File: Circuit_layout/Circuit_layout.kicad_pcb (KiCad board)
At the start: 2 copper layers, 168 parts, among them CON1 AVR-JTAG-10, J1 Spare_Conns, J10 AIRs, J3 CAN, J4 Motor_Ctrl, J5 RJ12, P1 TSV, P2 HVPL, P3 IMD, P4 GLV, P5 Cockpit, P6 Pedals, P7 BrakeLight/RTDS, Q1 MMBF170, Q2 MMBF170, Q3 BSS84, SW1 TS5A3159-Q1, U1 LM7332, U10 MCP2551-I/SN, U11 TLP293, U12 TLP293, U13 PDQ10-D, U14 PDQ15-D, U15 TLP293, U16 LTC3638, U17 MCP6004, U18 PDQ10-Q24-S12-D, U19 ACPL-C870, U2 LM7810CT, U20 ACPL-C870, U21 MCP6001, U3 MCP6004, U4 MCP6004, U5 LM7332, U6 LM339, U7 AT90CAN128-A, U8 74ACT11030, U9 TLP293, Y1 10MHz

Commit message: started working on throttle layout in pcb. added ch_gnd plane
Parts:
- removed C13, C36, C39: 0.1u, Capacitors_SMD:C_0805_HandSoldering
- removed C20: 15p, Capacitors_SMD:C_0805_HandSoldering
- removed C21, C9: 6.8uF, Capacitors_SMD:C_0805_HandSoldering
- removed C48: 10uF, Capacitors_SMD:C_0805_HandSoldering
- removed C8: 1uF, Capacitors_SMD:C_2220_HandSoldering
- removed R17: 150, Resistors_SMD:R_0805_HandSoldering
- removed R21: 1k, Resistors_SMD:R_0805_HandSoldering
- removed R85: 2k, Resistors_SMD:R_0805_HandSoldering
- removed R86: 100, Resistors_SMD:R_0805_HandSoldering
- removed U14: PDQ15-D, custom_footprints:PDQ_DCDC
- removed U4: MCP6004, Housings_SOIC:SOIC-14_3.9x8.7mm_Pitch1.27mm
- added HVPL_HV1: TEST_1P, Measurement_Points:Measurement_Point_Round-SMD-Pad_Big, F.Cu at (278.1, 29.2)
- added JP1: JUMPER3, Pin_Headers:Pin_Header_Straight_1x03_Pitch2.54mm, F.Cu at (78.7, 62.2)
- added L1: 100uH, Inductors:Inductor_Taiyo-Yuden_NR-80xx_HandSoldering, F.Cu at (247.7, 64.8)
- added R69: 250k, Resistors_SMD:R_0805_HandSoldering, F.Cu at (251.5, 43.2)
- added R70: 47k, Resistors_SMD:R_0805_HandSoldering, F.Cu at (260.4, 48.3)
- added R71: 330, Resistors_SMD:R_0805_HandSoldering, F.Cu at (188.0, 86.4)
- added R72: 330, Resistors_SMD:R_0805_HandSoldering, F.Cu at (153.7, 87.6)
- added R73: 330, Resistors_SMD:R_0805_HandSoldering, F.Cu at (158.8, 69.8)
- added R74: 330, Resistors_SMD:R_0805_HandSoldering, F.Cu at (153.7, 74.9)
- added R76: 750k, Resistors_SMD:R_0805_HandSoldering, F.Cu at (245.1, 55.9)
- added R77: 196k, Resistors_SMD:R_0805_HandSoldering, F.Cu at (251.5, 55.9)
- added SW2: TS5A3159-Q1, TO_SOT_Packages_SMD:SOT-23-6_Handsoldering, F.Cu at (-24.1, 139.7)
- added SW3: JS202011CQN, custom_footprints:CK_DPDT_Switch, F.Cu at (39.4, -11.4)
- added U22: TS372, Housings_SOIC:SOIC-8_3.9x4.9mm_Pitch1.27mm, F.Cu at (69.8, 88.9)
- added U23: TLP293, Housings_SSOP:SOP-4_4.4x2.8mm_Pitch1.27mm, F.Cu at (-17.8, 97.8)
- added U24: TLP293, Housings_SSOP:SOP-4_4.4x2.8mm_Pitch1.27mm, F.Cu at (-27.9, 97.8)
- added W1: I_Measure, Measurement_Points:Measurement_Point_Round-SMD-Pad_Big, F.Cu at (110.5, 31.8)
- added W10: Throttle_LPF, Measurement_Points:Measurement_Point_Round-SMD-Pad_Big, F.Cu at (31.8, 119.4)
- added W11: Throttle_LV, Measurement_Points:Measurement_Point_Round-SMD-Pad_Big, F.Cu at (-22.9, 149.9)
- added W12: V_Measure, Measurement_Points:Measurement_Point_Round-SMD-Pad_Big, F.Cu at (217.2, 71.1)
- added W13: Throttle_HV, Measurement_Points:Measurement_Point_Round-SMD-Pad_Big, F.Cu at (248.9, 134.6)
- added W14: +5HV, Measurement_Points:Measurement_Point_Round-SMD-Pad_Big, F.Cu at (227.3, 135.9)
- added W15: I/O_Ground, Measurement_Points:Measurement_Point_Round-SMD-Pad_Big, F.Cu at (232.4, 147.3)
- added W16: +24V, Measurement_Points:Measurement_Point_Round-SMD-Pad_Big, F.Cu at (66.0, 35.6)
- added W17: CH_GND, Measurement_Points:Measurement_Point_Square-SMD-Pad_Big, F.Cu at (55.9, 121.9)
- added W18: HV_GND, Measurement_Points:Measurement_Point_Square-SMD-Pad_Big, F.Cu at (257.8, 59.7)
- added W19: HVPL_LV, Measurement_Points:Measurement_Point_Round-SMD-Pad_Big, F.Cu at (247.7, 29.2)
- added W2: IMD_uC, Measurement_Points:Measurement_Point_Round-SMD-Pad_Big, F.Cu at (199.4, 96.5)
- added W20: GLV_GND, Measurement_Points:Measurement_Point_Square-SMD-Pad_Big, F.Cu at (55.9, 130.8)
- added W21: +5DC/DC_GND, Measurement_Points:Measurement_Point_Square-SMD-Pad_Big, F.Cu at (48.3, 130.8)
- added W22: +5DC/DC, Measurement_Points:Measurement_Point_Round-SMD-Pad_Big, F.Cu at (129.5, 111.8)
- added W23: V_Meas_GND, Measurement_Points:Measurement_Point_Square-SMD-Pad_Big, F.Cu at (48.3, 121.9)
- added W3: uC_GND, Measurement_Points:Measurement_Point_Square-SMD-Pad_Big, F.Cu at (38.1, 130.8)
- added W4: +10_GND, Measurement_Points:Measurement_Point_Square-SMD-Pad_Big, F.Cu at (33.0, 130.8)
- added W5: +10V, Measurement_Points:Measurement_Point_Round-SMD-Pad_Big, F.Cu at (-55.9, 114.3)
- added W6: APPS2_b, Measurement_Points:Measurement_Point_Round-SMD-Pad_Big, F.Cu at (-74.9, 147.3)
- added W7: APPS1_b, Measurement_Points:Measurement_Point_Round-SMD-Pad_Big, F.Cu at (-61.0, 114.3)
- added W8: Throttle_uC, Measurement_Points:Measurement_Point_Round-SMD-Pad_Big, F.Cu at (105.4, 99.1)
- added W9: Throttle_PL, Measurement_Points:Measurement_Point_Round-SMD-Pad_Big, F.Cu at (90.2, 67.3)
- C22: value DNP -> 0.1u
- C23: value 10uF -> 0.1u
- C24: value 15p -> 1uF; footprint Capacitors_SMD:C_0805_HandSoldering -> Capacitors_SMD:C_2220_HandSoldering
- C3: value 0.1u -> 2.2uF
- P7: value BrakeLight/RTDS -> RTDS; footprint custom_footprints:TerminalBlock_Pheonix_MPT-5.08mm_4pol -> custom_footprints:TerminalBlock_Pheonix_MPT-5.08mm_2pol
- Q1: value MMBF170 -> ZVP4525G; footprint TO_SOT_Packages_SMD:SOT-23 -> TO_SOT_Packages_SMD:SOT-223-3Lead_TabPin2
- Q3: value BSS84 -> MMBF170
- R1, R13, R22, R23, R28, R29, R3, R31, R4, R6, R7: value 1k -> 10k
- R14: value 47k -> 10k
- R16: value 2k -> 250k
- R18: value 100 -> 10k
- R19, R20: value 100 -> 250k
- R2: value 1k -> 250k
- R24, R30: value 1k -> 100k
- R39: value 750k -> 10k
- R42: value 196k -> 10k
- R51, R52: value 0 -> 250k
- R8: value 1M -> 10k
- SW1: value TS5A3159-Q1 -> SW_PUSH; footprint TO_SOT_Packages_SMD:SOT-23-6_Handsoldering -> custom_footprints:SW_RACON_8
- U1: value LM7332 -> PDM2-S24-S12; footprint Housings_SOIC:SOIC-8_3.9x4.9mm_Pitch1.27mm -> Converters_DCDC_ACDC:DCDC-Conv_TRACO_TMR_1-xxxx_Single
- U18: value PDQ10-Q24-S12-D -> TS912; footprint custom_footprints:PDQ_DCDC -> Housings_SOIC:SOIC-8_3.9x4.9mm_Pitch1.27mm
- U2: value LM7810CT -> MCP6002; footprint TO_SOT_Packages_THT:TO-220_Vertical -> Housings_SOIC:SOIC-8_3.9x4.9mm_Pitch1.27mm
- U5: value LM7332 -> LM7810CT; footprint Housings_SOIC:SOIC-8_3.9x4.9mm_Pitch1.27mm -> Power_Integrations:TO-220
- U6: value LM339 -> TS912; footprint Housings_SOIC:SOIC-14_3.9x8.7mm_Pitch1.27mm -> Housings_SOIC:SOIC-8_3.9x4.9mm_Pitch1.27mm
- moved C24 237.1 mm to (275.6, 49.5)
- moved U1 220.9 mm to (262.9, 17.8)
- moved R39 185.0 mm to (54.6, 82.5), turned to 270 degrees
- moved U18 181.5 mm to (52.1, 88.9)
- moved R42 178.1 mm to (59.7, 80.0)
- moved C23 177.5 mm to (55.9, 71.1)
- moved C15 118.1 mm to (-35.3, 109.9)
- moved R51 118.1 mm to (-13.0, 104.3)
- moved R52 118.1 mm to (-24.9, 115.4)
- moved C14 118.1 mm to (-40.3, 115.5)
- moved C44 118.1 mm to (-33.3, 104.3)
- moved R25 73.6 mm to (33.0, 92.7), turned to 90 degrees
- moved R30 72.2 mm to (44.5, 73.7)
- moved U2 67.6 mm to (96.5, 110.5)
- moved SW1 67.4 mm to (115.6, 63.5)
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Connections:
- C15 pad 1: APPS1 -> I_+5
- C16 pad 1: APPS2 -> Net-(C16-Pad1)
- C18 pad 1: +5V -> I_+5
- C22 pad 1: /Status Lights/BP_uC -> Net-(C22-Pad1)
- C23 pad 1: Net-(C19-Pad1) -> APPS1_10
- C23 pad 2: /Status Lights/HV- -> CH_GND
- C24 pad 1: Net-(C24-Pad1) -> /Status Lights/HV+
- C24 pad 2: CH_GND -> /Status Lights/HV-
- C25 pad 1: +5V -> I_+5
- C27 pad 1: +5V -> I_+5
- C3 pad 1: IMD_PWM -> HVPL
- C32 pad 1: +5V -> I_+5
- C33 pad 1: +5V -> I_+5
- C37 pad 1: +5V -> I_+5
- C38 pad 1: +5V -> APPS1_10
- C42 pad 1: +5V -> I_+5
- C43 pad 1: +5V -> I_+5
- C44 pad 1: +5V -> I_+5
- C45 pad 1: +5V -> I_+5
- C7 pad 1: +5V -> I_+5
- CON1 pad 4: +5V -> I_+5
- CON1 pad 7: Net-(CON1-Pad7) -> (no net)
- CON1 pad 8: Net-(CON1-Pad8) -> (no net)
- J5 pad 1: Net-(J5-Pad1) -> (no net)
- J5 pad 4: CH_GND -> I_RTN
- J5 pad 5: +5V -> I_+5
- J5 pad 6: Net-(J5-Pad6) -> (no net)
- P5 pad 3: +5V -> I_+5
- P6 pad 2: BP -> BOT
- P6 pad 3: APPS1_10 -> BP
- P6 pad 4: APPS2_5 -> APPS1_10
- P6 pad 5: APPS1_RTN -> APPS2_5
- P6 pad 6: CH_GND -> APPS1_RTN
- P6 pad 7: APPS1 -> CH_GND
- P6 pad 8: APPS2 -> APPS1
- P7 pad 1: Brake_Light -> RTDS
- P7 pad 2: RTDS -> CH_GND
- Q1 pad 2: CH_GND -> IMD_Fault_LED
- Q1 pad 3: Brake_Light -> +24V
- Q3 pad 2: IMD_Fault_LED -> CH_GND
- Q3 pad 3: +12V -> I_RTN
- R1 pad 1: CH_GND -> Net-(R1-Pad1)
- R1 pad 2: Net-(R1-Pad2) -> CH_GND
- R10 pad 1: +5V -> I_+5
- R11 pad 1: SDA -> SCL
- R11 pad 2: +5V -> I_+5
- R13 pad 1: Net-(Q1-Pad1) -> I_+5
- R13 pad 2: /Status Lights/BP_uC -> ~RESET_AVR
- R14 pad 1: Net-(R14-Pad1) -> Net-(Q3-Pad1)
- R14 pad 2: /Status Lights/HV- -> /I_ENB
- R16 pad 1: +24V -> Net-(R16-Pad1)
- R16 pad 2: Net-(R16-Pad2) -> /Status Lights/HV+
- R18 pad 1: +5V -> CH_GND
- R18 pad 2: Net-(D1-Pad2) -> Net-(Q3-Pad1)
- R19 pad 1: /Status Lights/Spare_Red -> Net-(R19-Pad1)
- R19 pad 2: Net-(D3-Pad2) -> Net-(R16-Pad1)
- R2 pad 1: Net-(R2-Pad1) -> AIRs+
- R2 pad 2: A1_LV -> Net-(R2-Pad2)
- R20 pad 1: /Status Lights/Spare_Blue -> Net-(R20-Pad1)
- R20 pad 2: Net-(D4-Pad2) -> Net-(R19-Pad1)
- R22 pad 1: Net-(R22-Pad1) -> /ThrottlePlausibility/APPS1_b
- R22 pad 2: +5V -> Net-(R22-Pad2)
- R23 pad 1: Net-(R21-Pad1) -> I_+5
- R23 pad 2: CH_GND -> Net-(R23-Pad2)
- R24 pad 1: /ThrottlePlausibility/APPS1_ISO -> APPS2
- R24 pad 2: Net-(R22-Pad1) -> Net-(C16-Pad1)
- R28 pad 1: Net-(R28-Pad1) -> Net-(R22-Pad2)
- R28 pad 2: APPS1 -> CH_GND
- R29 pad 1: Net-(R29-Pad1) -> Net-(R23-Pad2)
- R29 pad 2: APPS2 -> /ThrottlePlausibility/APPS1_ISO
- R3 pad 2: A2_LV -> A1_LV
- R30 pad 1: Net-(R28-Pad1) -> APPS1
- R30 pad 2: CH_GND -> Net-(C22-Pad1)
- R31 pad 1: Net-(R31-Pad1) -> /ThrottlePlausibility/APPS1_b
- R31 pad 2: Net-(R29-Pad1) -> Net-(R31-Pad2)
- R39 pad 1: Net-(C19-Pad1) -> /ThrottlePlausibility/APPS2_b
- R4 pad 1: Net-(R2-Pad1) -> Net-(R4-Pad1)
- R4 pad 2: CH_GND -> A2_LV
- R40 pad 1: Net-(C20-Pad1) -> Net-(R40-Pad1)
- R40 pad 2: +5V -> I_+5
- R41 pad 1: Net-(C24-Pad1) -> Net-(R41-Pad1)
- R41 pad 2: +5V -> I_+5
- R42 pad 1: Net-(R39-Pad2) -> Net-(R31-Pad2)
- R42 pad 2: /Status Lights/HV- -> CH_GND
- R43 pad 1: SCL -> /ThrottlePlausibility/Throttle_SEL
- R43 pad 2: +5V -> CH_GND
- R46 pad 2: APPS2 -> /ThrottlePlausibility/APPS2_b
- R47 pad 2: +5V -> I_+5
- R5 pad 2: +5V -> I_+5
- R50 pad 1: CH_GND -> Net-(R39-Pad2)
- R50 pad 2: BP -> Net-(R50-Pad2)
- R51 pad 2: /Status Lights/BP_uC -> Net-(R51-Pad2)
- R52 pad 1: CH_GND -> BOT
- R52 pad 2: CH_GND -> Net-(R52-Pad2)
- R6 pad 1: /I_Measure -> CH_GND
- R7 pad 1: Net-(R7-Pad1) -> /I_Measure
- R7 pad 2: AIRs+ -> Net-(R4-Pad1)
- R79 pad 2: +5V -> I_+5
- R8 pad 1: /Status Lights/HV+ -> SDA
- R8 pad 2: Net-(R14-Pad1) -> I_+5
- R82 pad 2: +5V -> I_+5
- R84 pad 1: Net-(Q3-Pad1) -> Net-(Q1-Pad1)
- SW1 pad 1: /ThrottlePlausibility/Pedal_Out -> ~RESET_AVR
- U1 pad 1: /ThrottlePlausibility/APPS1_ISO -> /Status Lights/HV-
- U1 pad 2: Net-(R22-Pad1) -> Net-(C19-Pad1)
- U1 pad 4: CH_GND -> (no net)
- U10 pad 3: +5V -> I_+5
- U10 pad 5: Net-(U10-Pad5) -> (no net)
- U11 pad 4: Net-(R16-Pad2) -> +24V
- U13 pad 3: +5V -> I_+5
- U13 pad 4: Net-(U13-Pad4) -> (no net)
- U13 pad 6: Net-(U13-Pad6) -> (no net)
- U15 pad 2: Net-(R1-Pad2) -> Net-(R1-Pad1)
- U16 pad 14: Net-(R14-Pad1) -> Net-(R69-Pad1)
- U16 pad 9: Net-(R39-Pad2) -> Net-(R76-Pad2)
- U17 pad 12: Net-(R79-Pad1) -> (no net)
- U17 pad 13: /ThrottlePlausibility/APPS1_ISO -> (no net)
- U17 pad 14: Net-(U17-Pad14) -> (no net)
- U17 pad 2: Net-(R3-Pad1) -> Net-(R4-Pad1)
- U17 pad 3: Net-(R2-Pad1) -> Net-(R3-Pad1)
- U17 pad 4: +5V -> I_+5
- U18 pad 1: /Status Lights/HV- -> /ThrottlePlausibility/APPS1_ISO
- U18 pad 2: Net-(C19-Pad1) -> Net-(R23-Pad2)
- U18 pad 3: /Status Lights/HVPL -> Net-(R22-Pad2)
- U18 pad 4: Net-(U18-Pad4) -> CH_GND
- U18 pad 5: CH_GND -> Net-(R31-Pad2)
- U18 pad 6: (no net) -> Net-(R39-Pad2)
- U19 pad 1: +5V -> I_+5
- U2 pad 1: +24V -> /ThrottlePlausibility/Pedal_Out
- U2 pad 2: CH_GND -> /ThrottlePlausibility/Pedal_Out
- U2 pad 3: APPS1_10 -> Net-(Q2-Pad3)
- U20 pad 8: +5V -> I_+5
- U3 pad 10: APPS2 -> Net-(R38-Pad1)
- U3 pad 12: (no net) -> /ThrottlePlausibility/APPS2_b
- U3 pad 13: (no net) -> Net-(R38-Pad2)
- U3 pad 14: (no net) -> Net-(U3-Pad14)
- U3 pad 2: Net-(R80-Pad2) -> /ThrottlePlausibility/APPS1_ISO
- U3 pad 3: /ThrottlePlausibility/APPS1_ISO -> Net-(R79-Pad1)
- U3 pad 4: +5V -> I_+5
- U3 pad 5: Net-(R38-Pad1) -> /ThrottlePlausibility/APPS1_ISO
- U3 pad 6: APPS2 -> Net-(R80-Pad2)
- U3 pad 9: Net-(R38-Pad2) -> /ThrottlePlausibility/APPS2_b
- U5 pad 1: Net-(R31-Pad1) -> +24V
- U5 pad 2: Net-(R29-Pad1) -> CH_GND
- U5 pad 3: Net-(R28-Pad1) -> APPS1_10
- U6 pad 1: Net-(C24-Pad1) -> /ThrottlePlausibility/APPS1_b
- U6 pad 2: Net-(C20-Pad1) -> /ThrottlePlausibility/APPS1_b
- U6 pad 3: APPS1_10 -> Net-(C22-Pad1)
- U6 pad 4: Net-(R31-Pad1) -> CH_GND
- U6 pad 5: Net-(R32-Pad1) -> Net-(C16-Pad1)
- U6 pad 6: Net-(R33-Pad1) -> /ThrottlePlausibility/APPS2_b
- U6 pad 7: Net-(R31-Pad1) -> /ThrottlePlausibility/APPS2_b
- U6 pad 8: (no net) -> APPS1_10
- U7 pad 10: Net-(U7-Pad10) -> (no net)
- U7 pad 11: Net-(U7-Pad11) -> (no net)
- U7 pad 12: Net-(U7-Pad12) -> (no net)
- U7 pad 13: Net-(U7-Pad13) -> (no net)
- U7 pad 14: /Status Lights/BP_uC -> /ThrottlePlausibility/BP_uC
- U7 pad 18: Net-(U7-Pad18) -> (no net)
- U7 pad 19: Net-(U7-Pad19) -> (no net)
- U7 pad 21: +5V -> I_+5
- U7 pad 27: Net-(U7-Pad27) -> (no net)
- U7 pad 28: Net-(U7-Pad28) -> (no net)
- U7 pad 29: Net-(U7-Pad29) -> (no net)
- U7 pad 32: Net-(U7-Pad32) -> (no net)
- U7 pad 33: Net-(U7-Pad33) -> (no net)
- U7 pad 34: Net-(U7-Pad34) -> (no net)
- U7 pad 35: Net-(U7-Pad35) -> /ThrottlePlausibility/BOT_uC
- U7 pad 39: Net-(U7-Pad39) -> (no net)
- U7 pad 4: Net-(U7-Pad4) -> (no net)
- U7 pad 40: Net-(U7-Pad40) -> (no net)
- U7 pad 41: Net-(U7-Pad41) -> (no net)
- U7 pad 42: Net-(U7-Pad42) -> (no net)
- U7 pad 43: Net-(U7-Pad43) -> (no net)
- U7 pad 44: Net-(U7-Pad44) -> /I_ENB
- U7 pad 45: Net-(U7-Pad45) -> (no net)
- U7 pad 49: Net-(U7-Pad49) -> (no net)
- U7 pad 50: Net-(U7-Pad50) -> (no net)
- U7 pad 51: /Safety_Loop -> (no net)
- U7 pad 52: +5V -> I_+5
- U7 pad 54: TDI -> /PIN54
- U7 pad 55: TDO -> /PIN55
- U7 pad 6: Net-(U7-Pad6) -> (no net)
- U7 pad 64: +5V -> I_+5
- U7 pad 7: Net-(U7-Pad7) -> /Safety_Loop
- U7 pad 8: Net-(U7-Pad8) -> (no net)
- U8 pad 1: +5V -> I_+5
- U8 pad 11: +5V -> I_+5
- U8 pad 12: Net-(U3-Pad1) -> Net-(U3-Pad7)
- U8 pad 13: Net-(U3-Pad7) -> Net-(U3-Pad8)
- U8 pad 14: Net-(U3-Pad8) -> Net-(U3-Pad14)
- U8 pad 2: +5V -> I_+5
- U8 pad 3: Net-(C20-Pad1) -> Net-(R40-Pad1)
- U8 pad 8: Net-(C24-Pad1) -> Net-(R41-Pad1)
- U8 pad 9: Net-(U17-Pad14) -> Net-(U3-Pad1)
- U9 pad 1: Net-(R7-Pad1) -> Net-(R2-Pad2)
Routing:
- net I_+5: track 0.00 -> 12.8 mm
- net /ThrottlePlausibility/APPS1_b: track 0.00 -> 9.92 mm
- net Net-(C16-Pad1): track 0.00 -> 8.84 mm
- net /ThrottlePlausibility/APPS2_b: track 0.00 -> 8.72 mm
- net /ThrottlePlausibility/Throttle_PL: track 0.00 -> 5.41 mm
- net Net-(Q2-Pad1): track 0.00 -> 3.81 mm
- net APPS1_10: track 0.00 -> 3.23 mm
- added copper zone on F.Cu, net CH_GND
- added copper zone on F.Cu, net HV-
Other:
- board outline added: 203.2 x 152.4 mm

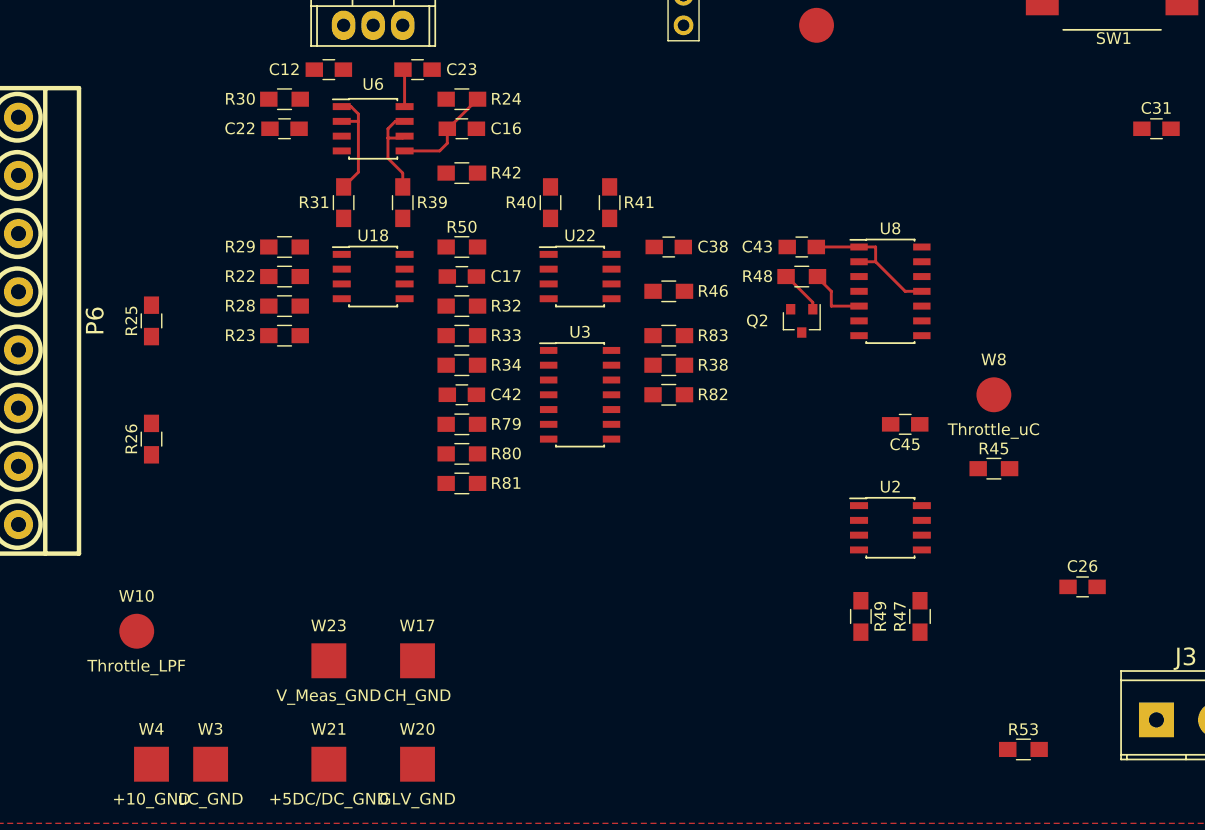
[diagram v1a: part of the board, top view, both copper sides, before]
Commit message: reviewed schematic w/ prof. nadovich. proposed changes
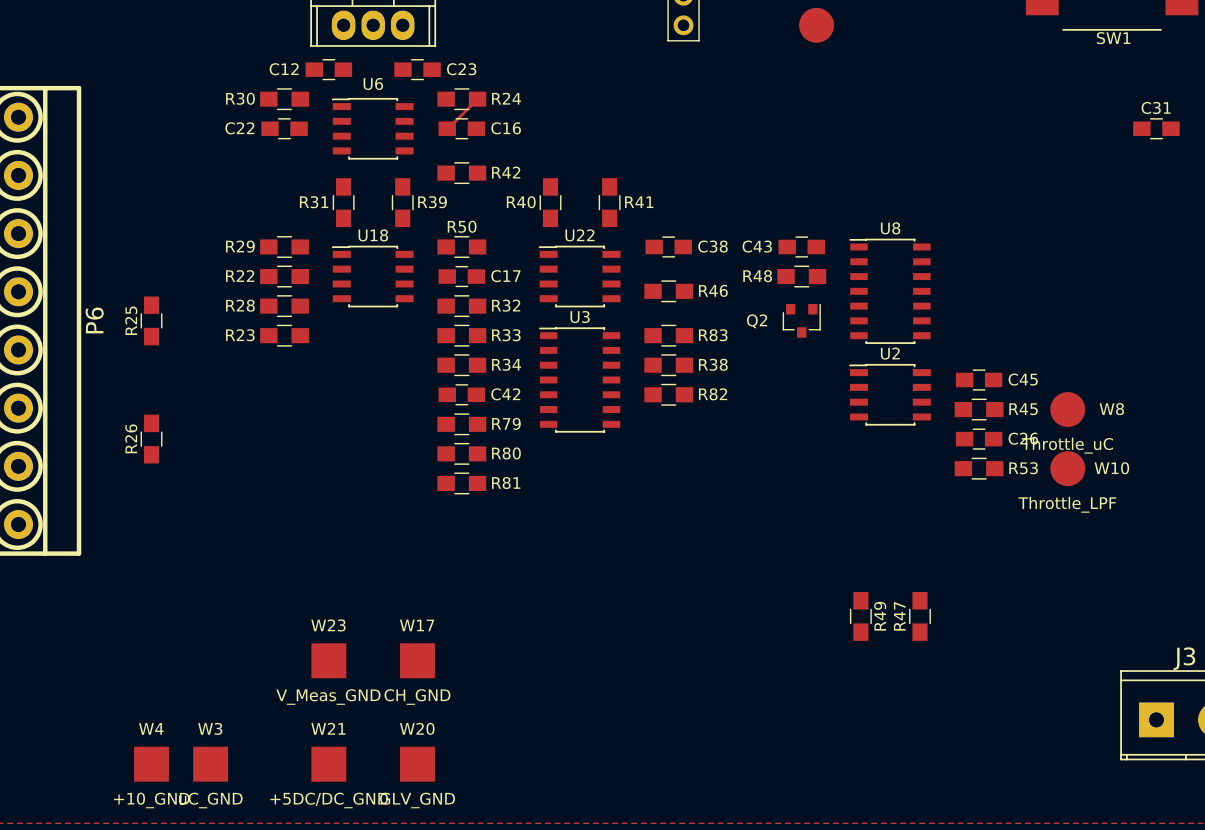
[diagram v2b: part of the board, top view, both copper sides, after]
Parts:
- moved W10 81.2 mm to (111.8, 105.4)
- moved R53 24.4 mm to (104.1, 105.4)
- moved C26 15.5 mm to (104.1, 102.9), turned to 180 degrees
- moved U2 11.4 mm to (96.5, 99.1)
- moved C45 7.41 mm to (104.1, 97.8), turned to 0 degrees
- moved W8 6.48 mm to (111.8, 100.3)
- moved R45 5.24 mm to (104.1, 100.3), turned to 180 degrees
- moved U3 1.27 mm to (69.8, 97.8)
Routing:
- net I_+5: track 12.8 -> 0.00 mm
- net /ThrottlePlausibility/APPS1_b: track 9.92 -> 0.00 mm
- net /ThrottlePlausibility/APPS2_b: track 8.72 -> 0.23 mm
- net /ThrottlePlausibility/Throttle_PL: track 5.41 -> 0.08 mm
- net Net-(C16-Pad1): track 8.84 -> 3.65 mm
- net Net-(Q2-Pad1): track 3.81 -> 0.08 mm
- net APPS1_10: track 3.23 -> 0.20 mm

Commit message: small changes
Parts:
- moved W18 130.4 mm to (170.2, 156.2)
- moved C40 89.8 mm to (175.6, 149.7)
- moved C41 89.8 mm to (179.3, 153.7)
- moved R60 89.8 mm to (183.1, 153.7)
- moved R61 89.8 mm to (186.9, 157.5)
- moved R65 89.8 mm to (193.2, 157.5)
- moved R67 89.8 mm to (199.6, 157.5)
- moved R68 89.8 mm to (205.9, 157.5)
- moved U20 68.4 mm to (185.4, 139.7), turned to 90 degrees
- moved C28 49.6 mm to (178.9, 115.8)
- moved C29 49.6 mm to (178.9, 130.8)
- moved C33 49.6 mm to (191.9, 128.8)
- moved R54 49.6 mm to (178.9, 120.8)
- moved R55 49.6 mm to (178.9, 125.8)
- moved R56 49.6 mm to (185.9, 125.8)
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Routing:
- net HV-: track 13.6 -> 0.14 mm
- net Net-(C41-Pad1): track 12.4 -> 0.14 mm
- net Net-(R67-Pad2): track 3.65 -> 0.00 mm
- net Net-(R61-Pad2): track 3.65 -> 0.00 mm
- net Net-(R65-Pad2): track 3.65 -> 0.00 mm
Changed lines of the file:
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@@
   (general
     (links 405)
-    (no_connects 330)
+    (no_connects 328)
     (area -78.419286 -19.055 282.071667 165.175001)
     (thickness 1.6)
     (drawings 9)
-    (tracks 24)
+    (tracks 9)
     (zones 0)
     (modules 193)
@@
     (pad_to_mask_clearance 0.2)
     (aux_axis_origin 0 0)
-    (visible_elements 7FFEFFFF)
+    (visible_elements 7FFEF7FF)
     (pcbplotparams
       (layerselection 0x00030_80000001)
@@
   )
   (module Capacitors_SMD:C_0805_HandSoldering (layer F.Cu)
-    (at 244.04 91.44 90)
+    (at 179.27 153.67 90)
     (descr "Capacitor SMD 0805, hand soldering")
     (tags "capacitor 0805")
@@
   )
   (module custom_footprints:Iso_Diff_Amp_ACPL (layer F.Cu)
-    (at 233.88 91.44 180)
+    (at 185.42 139.7 90)
     (descr "8-Lead Plastic Small Outline (SM) - Medium, 5.28 mm Body [SOIC] (see Microchip Packaging Specification 00000049BS.pdf)")
     (tags "SOIC 1.27")
     (attr smd)
-    (fp_text reference U20 (at 0 -3.68 180) (layer F.SilkS)
+    (fp_text reference U20 (at 0 -3.68 90) (layer F.SilkS)
       (effects (font (size 1 1) (thickness 0.15)))
     )
-    (fp_text value ACPL-C870 (at 0 3.68 180) (layer F.Fab)
+    (fp_text value ACPL-C870 (at 0 3.68 90) (layer F.Fab)
       (effects (font (size 1 1) (thickness 0.15)))
     )
@@
     (fp_line (start -2.75 -2.755) (end 2.75 -2.755) (layer F.SilkS) (width 0.15))
     (fp_line (start -2.75 2.755) (end 2.75 2.755) (layer F.SilkS) (width 0.15))
-    (pad 1 smd rect (at -5.3725 -1.905 180) (size 1.905 0.64) (layers F.Cu F.Paste F.Mask)
+    (pad 1 smd rect (at -5.3725 -1.905 90) (size 1.905 0.64) (layers F.Cu F.Paste F.Mask)
       (net 24 +5HV))
-    (pad 2 smd rect (at -5.3725 -0.635 180) (size 1.905 0.64) (layers F.Cu F.Paste F.Mask)
+    (pad 2 smd rect (at -5.3725 -0.635 90) (size 1.905 0.64) (layers F.Cu F.Paste F.Mask)
       (net 27 "Net-(C41-Pad1)"))
-    (pad 3 smd rect (at -5.3725 0.635 180) (size 1.905 0.64) (layers F.Cu F.Paste F.Mask)
+    (pad 3 smd rect (at -5.3725 0.635 90) (size 1.905 0.64) (layers F.Cu F.Paste F.Mask)
       (net 26 HV-))
-    (pad 4 smd rect (at -5.3725 1.905 180) (size 1.905 0.64) (layers F.Cu F.Paste F.Mask)
+    (pad 4 smd rect (at -5.3725 1.905 90) (size 1.905 0.64) (layers F.Cu F.Paste F.Mask)
       (net 26 HV-))
-    (pad 5 smd rect (at 5.3725 1.905 180) (size 1.905 0.65) (layers F.Cu F.Paste F.Mask)
+    (pad 5 smd rect (at 5.3725 1.905 90) (size 1.905 0.65) (layers F.Cu F.Paste F.Mask)
       (net 1 CH_GND))
-    (pad 6 smd rect (at 5.3725 0.635 180) (size 1.905 0.65) (layers F.Cu F.Paste F.Mask)
+    (pad 6 smd rect (at 5.3725 0.635 90) (size 1.905 0.65) (layers F.Cu F.Paste F.Mask)
       (net 81 "Net-(R57-Pad1)"))
-    (pad 7 smd rect (at 5.3725 -0.635 180) (size 1.905 0.64) (layers F.Cu F.Paste F.Mask)
+    (pad 7 smd rect (at 5.3725 -0.635 90) (size 1.905 0.64) (layers F.Cu F.Paste F.Mask)
       (net 21 "Net-(C29-Pad1)"))
-    (pad 8 smd rect (at 5.3725 -1.905 180) (size 1.905 0.64) (layers F.Cu F.Paste F.Mask)
+    (pad 8 smd rect (at 5.3725 -1.905 90) (size 1.905 0.64) (layers F.Cu F.Paste F.Mask)
       (net 108 I_+5))
     (model Housings_SOIC.3dshapes/SOIJ-8_5.3x5.3mm_Pitch1.27mm.wrl
@@
   )
   (module Capacitors_SMD:C_0805_HandSoldering (layer F.Cu)
-    (at 209 95)
+    (at 204.47 92.71)
     (descr "Capacitor SMD 0805, hand soldering")
     (tags "capacitor 0805")
@@
   )
   (module Capacitors_SMD:C_0805_HandSoldering (layer F.Cu)
-    (at 217 84)
+    (at 178.9 115.75)
     (descr "Capacitor SMD 0805, hand soldering")
     (tags "capacitor 0805")
@@
   )
   (module Capacitors_SMD:C_0805_HandSoldering (layer F.Cu)
-    (at 217 99 180)
+    (at 178.9 130.75 180)
     (descr "Capacitor SMD 0805, hand soldering")
     (tags "capacitor 0805")
@@
   )
   (module Capacitors_SMD:C_0805_HandSoldering (layer F.Cu)
-    (at 230 97 180)
+    (at 191.9 128.75 180)
     (descr "Capacitor SMD 0805, hand soldering")
     (tags "capacitor 0805")
@@
   )
   (module Capacitors_SMD:C_0805_HandSoldering (layer F.Cu)
-    (at 240.4 87.5 180)
+    (at 175.63 149.73 180)
     (descr "Capacitor SMD 0805, hand soldering")
     (tags "capacitor 0805")
@@
   )
   (module Resistors_SMD:R_0805_HandSoldering (layer F.Cu)
-    (at 217 89)
+    (at 178.9 120.75)
     (descr "Resistor SMD 0805, hand soldering")
     (tags "resistor 0805")
@@
   )
   (module Resistors_SMD:R_0805_HandSoldering (layer F.Cu)
-    (at 217 94)
+    (at 178.9 125.75)
     (descr "Resistor SMD 0805, hand soldering")
     (tags "resistor 0805")
@@
   )
   (module Resistors_SMD:R_0805_HandSoldering (layer F.Cu)
-    (at 224 94 180)
+    (at 185.9 125.75 180)
     (descr "Resistor SMD 0805, hand soldering")
     (tags "resistor 0805")
@@
   )
   (module Resistors_SMD:R_0805_HandSoldering (layer F.Cu)
-    (at 224 89 180)
+    (at 185.9 120.75 180)
     (descr "Resistor SMD 0805, hand soldering")
     (tags "resistor 0805")
@@
   )
   (module Resistors_SMD:R_0805_HandSoldering (layer F.Cu)
-    (at 247.85 91.44 270)
+    (at 183.08 153.67 270)
     (descr "Resistor SMD 0805, hand soldering")
     (tags "resistor 0805")
@@
   )
   (module Resistors_SMD:R_0805_HandSoldering (layer F.Cu)
-    (at 251.66 95.25)
+    (at 186.89 157.48)
     (descr "Resistor SMD 0805, hand soldering")
     (tags "resistor 0805")
@@
   )
   (module Resistors_SMD:R_0805_HandSoldering (layer F.Cu)
-    (at 258.01 95.25)
+    (at 193.24 157.48)
     (descr "Resistor SMD 0805, hand soldering")
     (tags "resistor 0805")
@@
   )
   (module Resistors_SMD:R_0805_HandSoldering (layer F.Cu)
-    (at 264.36 95.25)
+    (at 199.59 157.48)
     (descr "Resistor SMD 0805, hand soldering")
     (tags "resistor 0805")
@@
   )
   (module Resistors_SMD:R_0805_HandSoldering (layer F.Cu)
-    (at 270.71 95.25)
+    (at 205.94 157.48)
     (descr "Resistor SMD 0805, hand soldering")
     (tags "resistor 0805")
@@
   )
   (module Measurement_Points:Measurement_Point_Square-SMD-Pad_Big (layer F.Cu)
-    (at 55.88 121.92)
+    (at 68.58 121.92)
     (descr "Mesurement Point, Square, SMD Pad,  3mm x 3mm,")
     (tags "Mesurement Point Square SMD Pad 3x3mm")
@@
   )
   (module Measurement_Points:Measurement_Point_Square-SMD-Pad_Big (layer F.Cu)
-    (at 257.81 59.69)
+    (at 170.18 156.21)
     (descr "Mesurement Point, Square, SMD Pad,  3mm x 3mm,")
     (tags "Mesurement Point Square SMD Pad 3x3mm")
@@
     (arrow2b (pts (xy 12.7 0) (xy 13.826504 -0.586421)))
   )
+  (segment (start 174.38 151.6625) (end 174.4825 151.765) (width 0.25) (layer F.Cu) (net 0) (status 30))
   (segment (start 54.77 71.26) (end 54.63 71.12) (width 0.25) (layer F.Cu) (net 15))
-  (segment (start 239.15 87.5) (end 239.15 89.4325) (width 0.25) (layer F.Cu) (net 26))
-  (segment (start 239.15 89.4325) (end 239.2525 89.535) (width 0.25) (layer F.Cu) (net 26))
-  (segment (start 244.04 90.19) (end 247.75 90.19) (width 0.25) (layer F.Cu) (net 26))
-  (segment (start 247.75 90.19) (end 247.85 90.09) (width 0.25) (layer F.Cu) (net 26))
-  (segment (start 239.2525 89.535) (end 240.955 89.535) (width 0.25) (layer F.Cu) (net 26) (status 10))
-  (segment (start 240.955 89.535) (end 241.61 90.19) (width 0.25) (layer F.Cu) (net 26))
-  (segment (start 239.2525 90.805) (end 240.995 90.805) (width 0.25) (layer F.Cu) (net 26) (status 10))
-  (segment (start 241.61 90.19) (end 244.04 90.19) (width 0.25) (layer F.Cu) (net 26))
-  (segment (start 240.995 90.805) (end 241.61 90.19) (width 0.25) (layer F.Cu) (net 26))
-  (segment (start 244.04 92.69) (end 247.75 92.69) (width 0.25) (layer F.Cu) (net 27))
-  (segment (start 247.75 92.69) (end 247.85 92.79) (width 0.25) (layer F.Cu) (net 27))
-  (segment (start 244.04 92.69) (end 242.89 92.69) (width 0.25) (layer F.Cu) (net 27))
-  (segment (start 242.275 92.075) (end 239.2525 92.075) (width 0.25) (layer F.Cu) (net 27) (status 20))
-  (segment (start 242.89 92.69) (end 242.275 92.075) (width 0.25) (layer F.Cu) (net 27))
-  (segment (start 250.31 95.25) (end 247.85 92.79) (width 0.25) (layer F.Cu) (net 27))
+  (segment (start 182.98 152.42) (end 183.08 152.32) (width 0.25) (layer F.Cu) (net 26))
+  (segment (start 182.98 154.92) (end 183.08 155.02) (width 0.25) (layer F.Cu) (net 27))
   (segment (start 87.63 88.9) (end 87.55 88.9) (width 0.25) (layer F.Cu) (net 51))
   (segment (start 90.25 88.9) (end 90.25 88.98) (width 0.25) (layer F.Cu) (net 78))
-  (segment (start 253.01 95.25) (end 256.66 95.25) (width 0.25) (layer F.Cu) (net 83))
-  (segment (start 259.36 95.25) (end 263.01 95.25) (width 0.25) (layer F.Cu) (net 86))
-  (segment (start 265.71 95.25) (end 269.36 95.25) (width 0.25) (layer F.Cu) (net 87) (status 20))
   (segment (start 58.44 76.2) (end 58.5 76.2) (width 0.25) (layer F.Cu) (net 109))
   (segment (start 58.5 76.2) (end 61.04 73.66) (width 0.25) (layer F.Cu) (net 109))

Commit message: continued work on layout of pcb
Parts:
- moved R8 157.9 mm to (120.0, 94.0)
- moved R70 154.3 mm to (148.3, 154.4)
- moved R69 153.9 mm to (148.3, 157.5)
- moved C34 152.3 mm to (96.5, 148.6), turned to 180 degrees
- moved U1 151.7 mm to (192.0, 151.9), turned to 90 degrees
- moved C19 151.0 mm to (166.6, 150.9)
- moved U16 150.5 mm to (148.8, 148.3), turned to 90 degrees
- moved R14 150.2 mm to (126.4, 103.5), turned to 180 degrees
- moved C47 149.4 mm to (90.2, 157.5)
- moved D5 147.6 mm to (143.3, 148.3)
- moved U21 147.1 mm to (96.5, 152.4), turned to 0 degrees
- moved R64 146.8 mm to (96.5, 158.8)
- moved R62 145.1 mm to (90.2, 152.4), turned to 180 degrees
- moved R63 144.6 mm to (90.2, 154.9)
- moved R66 143.7 mm to (96.5, 156.2), turned to 0 degrees
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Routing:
- net /ThrottlePlausibility/APPS2_b: track 0.23 -> 51.0 mm, vias 0 -> 9
- net Net-(R31-Pad2): track 0.00 -> 23.4 mm, vias 0 -> 3
- net /ThrottlePlausibility/APPS1_b: track 0.00 -> 23.2 mm, vias 0 -> 6
- net Net-(R33-Pad1): track 0.00 -> 22.2 mm, vias 0 -> 7
- net APPS1_10: track 0.20 -> 19.4 mm, vias 0 -> 4
- net Net-(C41-Pad1): track 0.14 -> 17.8 mm, vias 0 -> 5
- net Net-(R23-Pad2): track 0.00 -> 17.2 mm, vias 0 -> 4
- net Net-(R39-Pad2): track 0.00 -> 17.1 mm, vias 0 -> 4
- net Net-(R50-Pad2): track 0.00 -> 16.1 mm, vias 0 -> 4
- net Net-(R79-Pad1): track 0.00 -> 14.0 mm, vias 0 -> 4
- net Net-(R32-Pad1): track 0.00 -> 10.9 mm, vias 0 -> 4
- net Net-(R63-Pad1): track 0.00 -> 10.2 mm, vias 0 -> 2
- net +5HV: track 0.00 -> 9.19 mm, vias 0 -> 4
- net Net-(C46-Pad1): track 0.00 -> 8.38 mm, vias 0 -> 2
- net Net-(C22-Pad1): track 0.00 -> 6.76 mm, vias 0 -> 2
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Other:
- board text added: "Update U5 to have horizontal footprint"
